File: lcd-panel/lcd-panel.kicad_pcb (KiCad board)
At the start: 2 copper layers, 85 x 26 mm, 46 parts, among them J1 USB wire, J2 LCD FPC connector, J3 Fan Socket, J4 TC2030, Q1 AO3400A, Q2 AO3401A, Q3 AO3400A, U1 FT232HL-REEL, U2 93LC56BT-I/OT, U3 USBLC6-2SC6, U4 ATtiny414-SS, Y1 12 MHz, 20 pF load

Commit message: Spit and polish
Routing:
- net GND: track 8.79 -> 33.0 mm, vias 2 -> 35
- net +3V3: track 83.5 -> 90.3 mm, vias 2 -> 4
- net +5V: track 68.4 -> 65.7 mm, vias 3 -> 4
- net D+: track 19.7 -> 20.9 mm
- net MISO: track 23.5 -> 22.8 mm

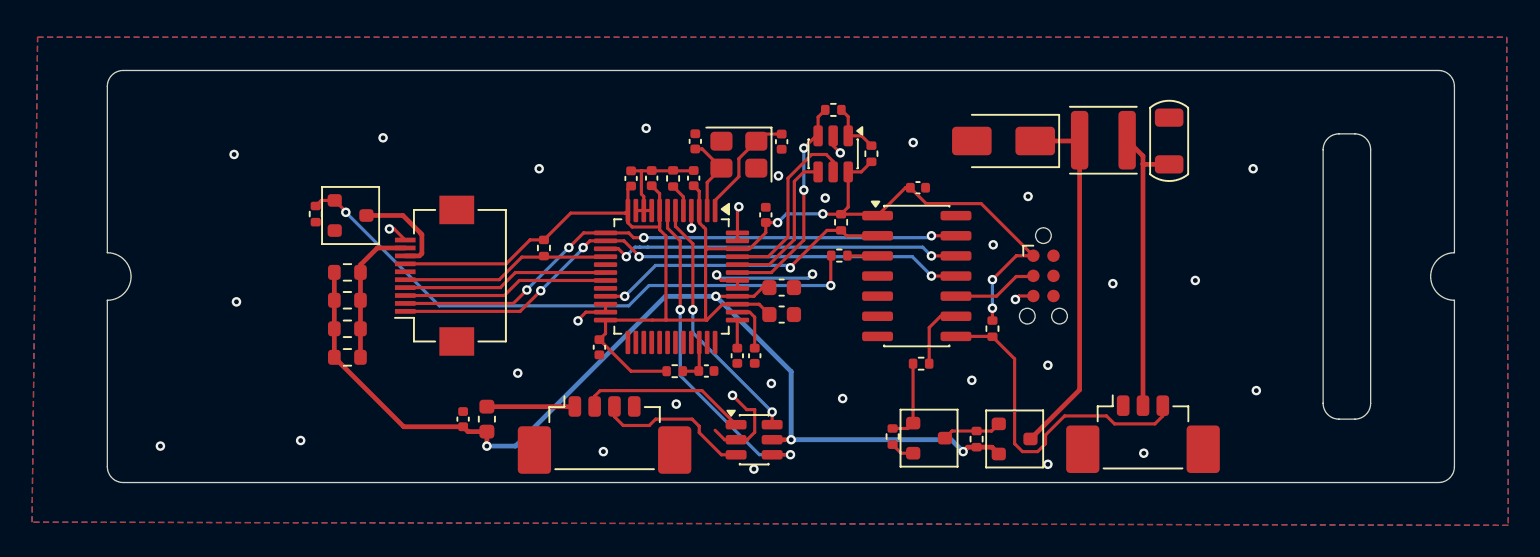
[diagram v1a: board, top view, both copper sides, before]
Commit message: Reworking the PCB components placeent
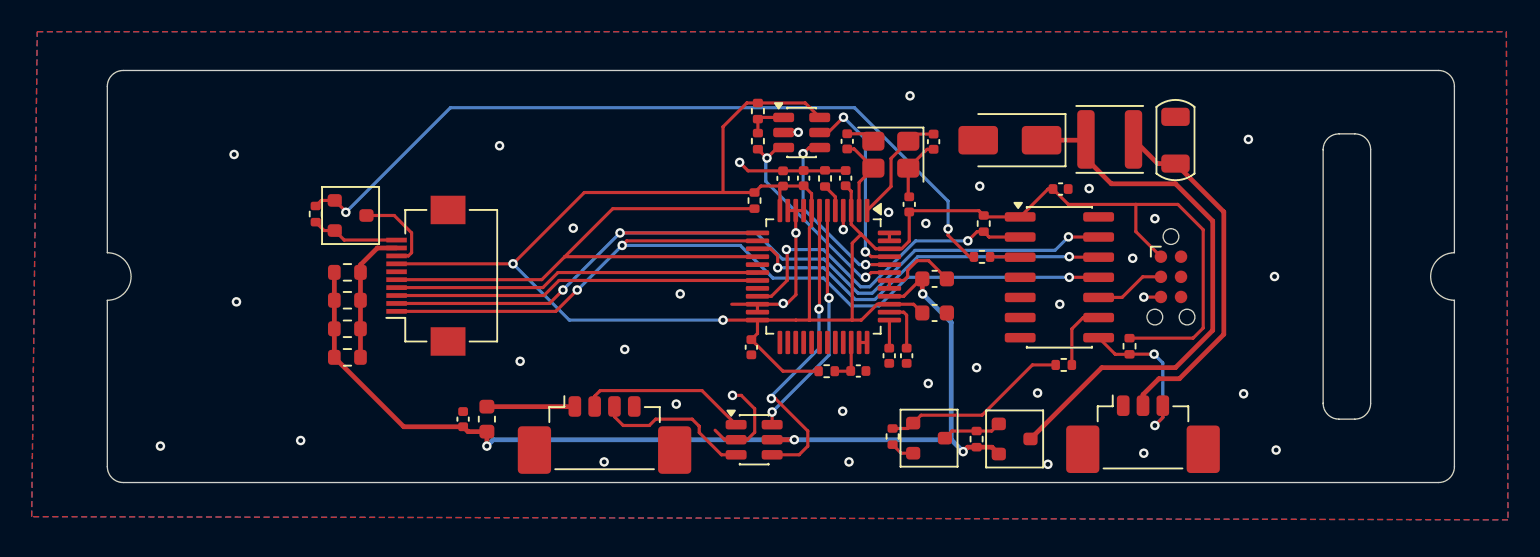
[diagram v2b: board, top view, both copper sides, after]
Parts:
- moved R11 13.6 mm to (132.3, 95.2)
- moved C1 9.67 mm to (143.7, 100.2)
- moved C8 9.65 mm to (143.7, 102.3)
- moved C10 9.59 mm to (138.0, 93.8)
- moved C12 9.59 mm to (140.8, 105.0)
- moved C13 9.59 mm to (138.8, 106.0)
- moved C3 9.59 mm to (143.6, 91.5)
- moved C4 9.59 mm to (134.1, 93.8)
- moved C5 9.59 mm to (132.1, 104.5)
- moved R1 9.59 mm to (136.7, 93.8)
- moved R4 9.59 mm to (136.8, 106.0)
- moved C7 9.59 mm to (135.4, 93.8)
- moved U1 9.59 mm to (136.6, 100.0)
- moved C11 9.59 mm to (141.9, 105.0)
- moved C2 9.59 mm to (138.1, 91.5)
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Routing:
- net +3V3: track 90.3 -> 133.9 mm, vias 4 -> 2
- net LCD_CS: track 13.2 -> 36.6 mm
- net SCK: track 36.8 -> 57.9 mm, vias 4 -> 3
- net MOSI: track 37.6 -> 57.0 mm, vias 4 -> 3
- net GND: track 33.0 -> 46.7 mm, vias 35 -> 37
- net Net-(Q3-G): track 37.9 -> 49.9 mm
- net Net-(D1-K): track 23.0 -> 34.9 mm
- net TACH: track 21.5 -> 10.3 mm, vias 0 -> 2
- net LCD_RST: track 13.0 -> 23.2 mm
- net LCD_DC: track 13.0 -> 23.2 mm
- net Net-(Q1-G): track 5.19 -> 12.0 mm
- net /Fan VDD: track 18.8 -> 22.7 mm
- net /SS TINY: track 19.2 -> 21.6 mm
- net EECLK: track 9.66 -> 11.6 mm, vias 0 -> 2
- net MISO: track 22.8 -> 24.4 mm
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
